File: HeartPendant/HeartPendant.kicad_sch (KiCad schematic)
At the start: 27 parts, among them J1 USB_C_Receptacle_USB2.0_16P, J2 Bat +, J3 Bat -, SW1 SW_Boot, SW2 SW_SPDT, U1 ESP32-C3-MINI-1-N4X, U2 USBLC6-2SC6, U3 MCP73831-2-OT, U4 AP2112K-3.3

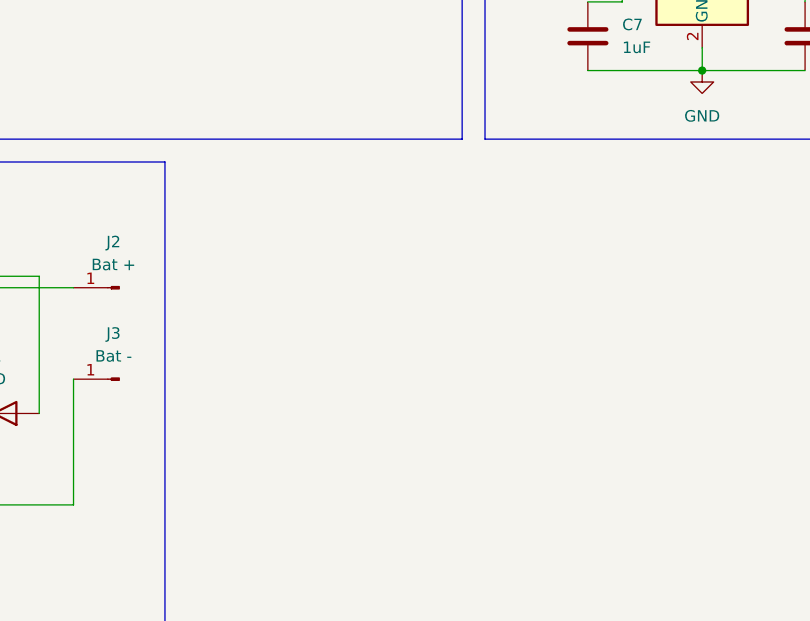
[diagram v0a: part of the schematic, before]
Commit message: Added: Added the pulse sensor module
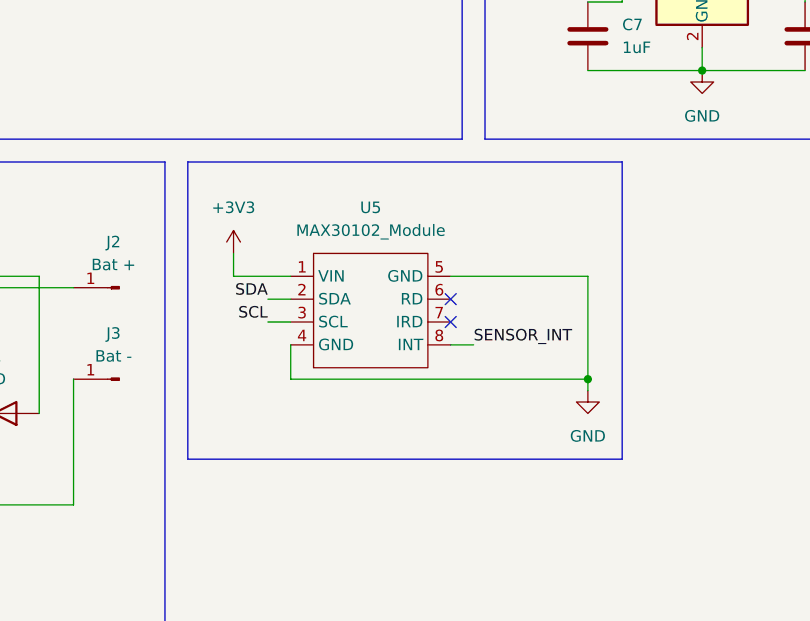
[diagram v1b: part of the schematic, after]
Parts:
- added U5: MAX30102_Module, symbol Components_HP:MAX30102_Module
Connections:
- net +3V3: now also U5.1 (VIN)
- net GND: now also U5.4 (GND), U5.5 (GND)
- net SCL: now also U5.3 (SCL)
- net SDA: now also U5.2 (SDA)
- net SENSOR_INT: now also U5.8 (INT)
- no-connect marks 23 -> 25

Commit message: Added: added LED array, and LED power managment
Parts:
- renumbered C3 to C1, C6 to C3, C1 to C5, C5 to C6, J2 to J1, J3 to J2, J1 to J3, R8 to R1, R9 to R2, R6 to R4, R1 to R5, R2 to R6, R4 to R8, R5 to R9, U3 to U1, U1 to U2, U5 to U3, U2 to U5
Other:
- added sheet Pendant (Pendant.kicad_sch)
- moved on the sheet: C1, C2, C3, C4, C5, C6, C7, C8, D1, J1, J2, J3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

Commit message: Added: Started on PCB, made custom outline, finished routing Bracelet
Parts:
- removed J1: Bat +, Package_TO_SOT_SMD:SOT-23-5, symbol Connector:Conn_01x01_Pin
- removed J2: Bat -, Package_TO_SOT_SMD:SOT-23-5, symbol Connector:Conn_01x01_Pin
- added J1: Bat, Connector_PinHeader_2.54mm:PinHeader_1x02_P2.54mm_Vertical, symbol Connector:Conn_01x02_Pin
- C1, C5: footprint (none) -> Capacitor_SMD:C_0603_1608Metric
- C2: footprint (none) -> Capacitor_SMD:C_0805_2012Metric
- C3, C4, C6, C7, C8: footprint Package_TO_SOT_SMD:SOT-23-5 -> Capacitor_SMD:C_0603_1608Metric
- D1: footprint LED_SMD:LED_Cree-XHP50_3V_HighDensity -> LED_SMD:LED_0603_1608Metric
- J2: renamed from J3; footprint Package_DFN_QFN:WDFN-10-1EP_3x3mm_P0.5mm_EP1.8x2.5mm -> Connector_USB:USB_C_Receptacle_HRO_TYPE-C-31-M-12
- R1, R2, R4, R7, R8, R9: footprint (none) -> Resistor_SMD:R_0603_1608Metric
- R3, R5, R6: footprint RF_Module:ESP32-C3-DevKitM-1 -> Resistor_SMD:R_0603_1608Metric
- SW1: footprint Package_DIP:DIP-24_W7.62mm -> HX_Push_SW:SW-SMD_4P-L4.2-W3.4-P2.15-LS5.2
- SW2: footprint Button_Switch_THT:SW_Slide-03_Wuerth-WS-SLTV_10x2.5x6.4_P2.54mm -> MSK12C02:SW-TH_MSK12C02
- U3: footprint (none) -> HeartPendant:Max30102_Module
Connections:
- net GND: now also J1.1 (Pin_1)
- net VBAT: now also J1.2 (Pin_2)

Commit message: Finished pendant routing, added production files
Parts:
- C1, C7, C8: LCSC Part (none) -> C1592
- C2: LCSC Part (none) -> C1713
- C3, C4, C6: LCSC Part (none) -> C1705
- C5: LCSC Part (none) -> C1590
- D1: LCSC Part (none) -> C2286
- J1, U3: now not fitted; now left out of the parts list
- J2: LCSC Part (none) -> C165948
- R1, R2: LCSC Part (none) -> C14675
- R3, R4, R5, R6: LCSC Part (none) -> C15401
- R7: LCSC Part (none) -> C23179
- R8, R9: LCSC Part (none) -> C14677
- SW1: LCSC Part (none) -> C55200589
- SW2: LCSC Part (none) -> C431540
- U1: LCSC Part (none) -> C14879
- U4: LCSC Part (none) -> C51118
- U5: LCSC Part (none) -> C7519
